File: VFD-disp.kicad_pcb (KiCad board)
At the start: 4 copper layers, 99.6 x 65.5 mm, 118 parts, among them J1 USB_C_Receptacle_USB2.0_14P, J2 Conn_02x03_Odd_Even, J4 Conn_02x03_Odd_Even, J5 Conn_02x03_Odd_Even, J6 Conn_02x03_Odd_Even, Q1 Q_NMOS_GDS, Q2 Q_NMOS_GDS, Q3 Q_NPN_BEC, SW1 SW_SPST, U1 ESP32-C6-WROOM-1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

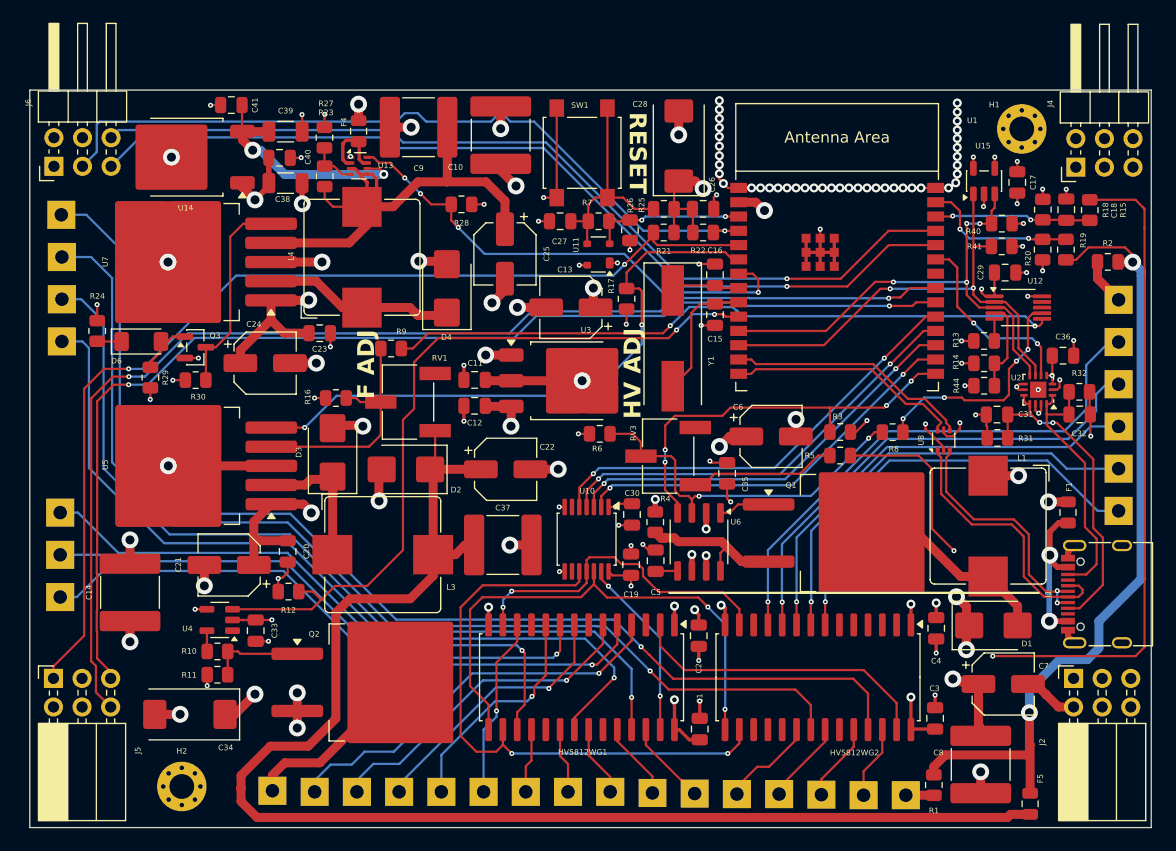
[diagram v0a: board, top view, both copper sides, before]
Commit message: Fix docking connectors reroute usb
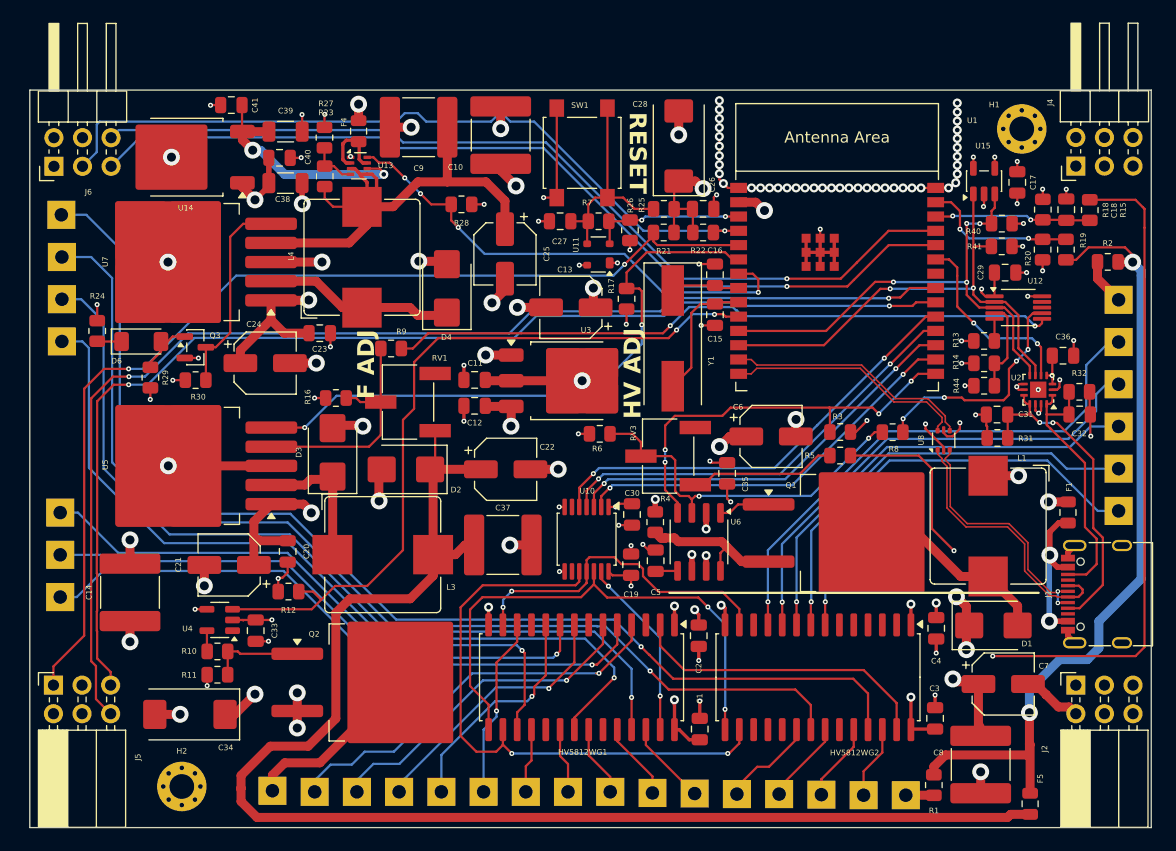
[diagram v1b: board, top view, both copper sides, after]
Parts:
- moved J2 0.63 mm to (132.0, 242.1)
- moved J5 0.60 mm to (41.2, 242.1)
- moved J4 0.10 mm to (132.0, 196.0)
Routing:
- net TX2: track 103.5 -> 104.1 mm
- net BACKWARD_DETECT: track 91.8 -> 92.4 mm
- net RX2: track 107.2 -> 107.8 mm

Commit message: Fix silkscreen and plot gerber
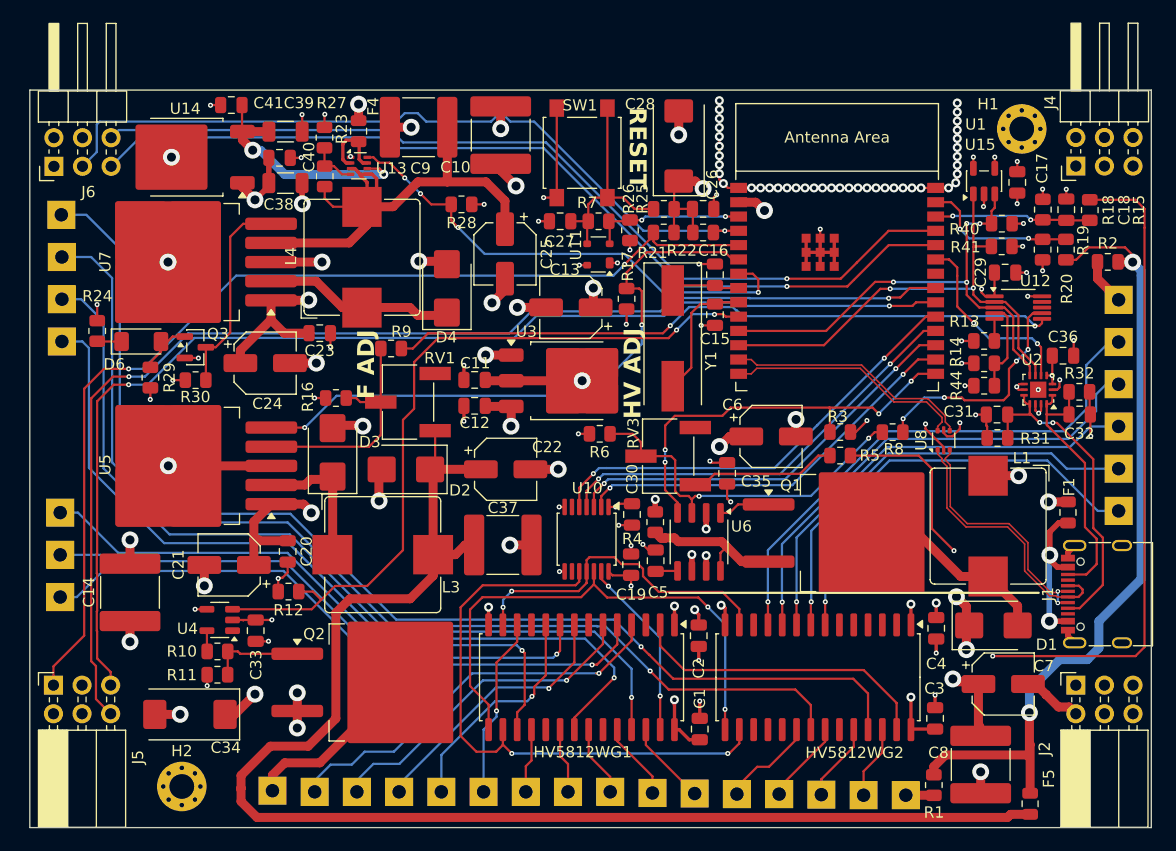
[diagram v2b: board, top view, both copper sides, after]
